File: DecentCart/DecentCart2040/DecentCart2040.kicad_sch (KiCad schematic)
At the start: 74 parts, among them J1 Micro_SD_Card, J2 Conn_02x15_Row_Letter_First, J3 SM03B-SRSS-TB, J7 Conn_01x04, J8 USB_B_Micro, J9 SM03B-SRSS-TB, Q2 TP0610L, SW2 SW_TACTILE, SW3 SW_TACTILE, U1 SN74LVC8T245, U2 SN74LVC8T245, U3 ATtiny1616-M, U4 NCP1117-3.3, U5 SN74LVC8T245, U6 SN74AVC4T245PW, U7 RP2040, U9 W25Q128JVS, X1 12MHz

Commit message: DecentCart 2040 rev. 1.1 fixes
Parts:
- added D3: MBR120VLSFT1G, Diode_SMD:Nexperia_CFP3_SOD-123W, symbol Device:D_Schottky
- Q2: value TP0610L -> DMG2305UX; JLCPCB Part # C10487 -> C150470
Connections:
- net +3V3: now also C14.1
- net +5V HOST: now also C18.2, C19.2, C2.2, C3.2, C30.2, C31.2, C39.2, C40.2, U1.23 (V_{CCB}), U1.24 (V_{CCB}), U2.23 (V_{CCB}), U2.24 (V_{CCB}), U5.23 (V_{CCB}), U5.24 (V_{CCB}), U6.16 (VCCB)
- net GND: now also C14.2
- net GPIO28: now also J7.4 (Pin_4), U3.13 (PB1); no longer J7.3 (Pin_3), U3.14 (PB0)
- net GPIO29: now also J7.3 (Pin_3), U3.14 (PB0); no longer J7.4 (Pin_4), U3.13 (PB1)
- net VBUS: now also D3.2 (A); no longer C26.1, U4.3 (VI)
- removed net +5V: C18.2, C19.2, C2.2, C3.2, C30.2, C31.2, C39.2, C40.2, Q2.1 (S), U1.23 (V_{CCB}), U1.24 (V_{CCB}), U2.23 (V_{CCB}), U2.24 (V_{CCB}), U5.23 (V_{CCB}), U5.24 (V_{CCB}), U6.16 (VCCB)
- new net VSYS: C26.1, D3.1 (K), Q2.1 (S), U4.3 (VI)
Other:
- note removed: "Only use to flash firmware"
- moved on the sheet: C14, Q2

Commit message: DecentCart2040 rev. 1.1
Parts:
- removed U6: SN74AVC4T245PW, Package_SO:TSSOP-16_4.4x5mm_P0.65mm, symbol Logic_LevelTranslator:SN74AVC4T245PW
- added C15, C20: 100nF, Capacitor_SMD:C_0402_1005Metric, symbol Device:C_Small
- added C21: 1uF, Capacitor_SMD:C_0402_1005Metric, symbol Device:C_Small
- added J4: Conn_01x08_Pin, Connector_PinHeader_1.27mm:PinHeader_2x04_P1.27mm_Vertical, symbol Connector:Conn_01x08_Pin
- added U6, U8: SN74LVC2T45DCUR, Package_SO:VSSOP-8_2.3x2mm_P0.5mm, symbol Logic_LevelTranslator:SN74LVC2T45DCUR
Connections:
- net +3V3: now also J3.2 (Pin_2), C15.2, U6.1 (VCCA), U8.1 (VCCA); no longer J3.1 (Pin_1)
- net +5V HOST: now also C20.2, C21.2, U6.8 (VCCB), U8.8 (VCCB)
- net /S4: now also U6.7 (B1)
- net /S5: now also U6.6 (B2)
- net GND: now also J3.3 (Pin_3), C15.1, C20.1, C21.1, U6.4 (GND), U8.4 (GND); no longer J3.2 (Pin_2)
- net GPIO23: now also R1.1
- net GPIO24: now also U6.2 (A1)
- net GPIO25: now also U6.3 (A2)
- net GPIO26: now also U8.2 (A1)
- net GPIO27: now also U8.3 (A2)
- net LVL_EN: now also J4.8 (Pin_8)
- net R/W: no longer R1.1
- net RD4: now also U8.7 (B1)
- net RD5: now also U8.6 (B2)
- net at U3.10 (PB4): now also J4.7 (Pin_7)
- net at U3.11 (PB3): now also J4.6 (Pin_6); no longer D2.1 (K)
- net at U3.12 (PB2): now also J4.5 (Pin_5); no longer R10.1
- net at U3.15 (PC0): now also J4.1 (Pin_1)
- net at U3.16 (PC1): now also J4.2 (Pin_2)
- net at U3.17 (PC2): now also J4.3 (Pin_3)
- net at U3.18 (PC3): now also J4.4 (Pin_4)
- net at U3.19 (~{RESET}/PA0): now also J3.1 (Pin_1); no longer J3.3 (Pin_3)
- net at U3.6 (PA5): now also J1.9 (DET)
- net at U3.7 (PA6): now also R10.1
- net at U3.8 (PA7): now also D1.2 (A), D2.1 (K)
- net at D1.1 (K), D2.2 (A): now also R10.2
- net at R2.2: now also U6.5 (DIR)
- net at R3.2: now also U8.5 (DIR)
- no-connect marks 10 -> 1
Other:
- note added: "Address & Control"
- note added: "Bank Shifting"
- note added: "RP2040"
- note removed: "Address"
- note removed: "I/O"
- moved on the sheet: C1, C10, C11, C12, C13, C14, C16, C17, C18, C19, C2, C23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

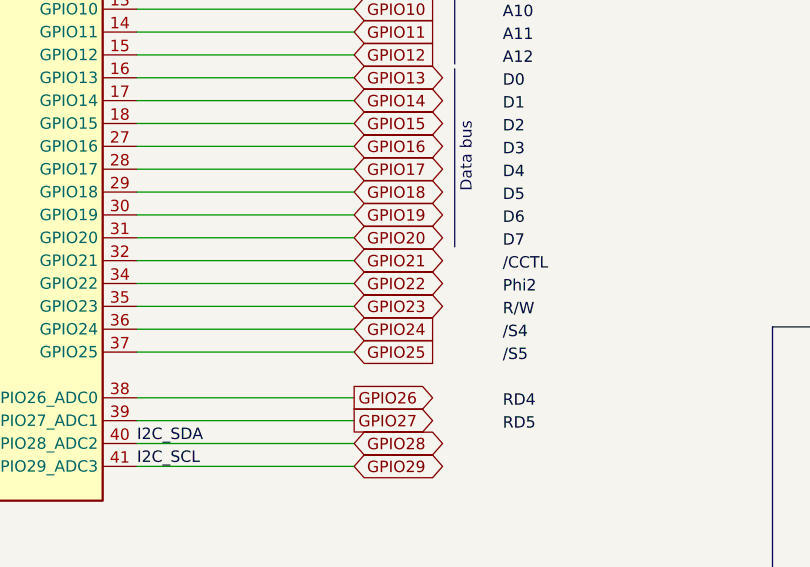
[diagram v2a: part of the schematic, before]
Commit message: DecentCart 2350 component placement
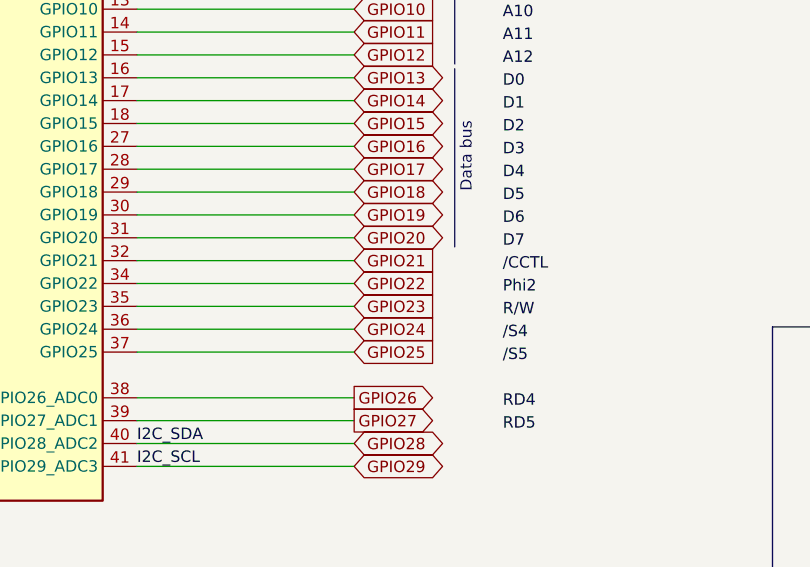
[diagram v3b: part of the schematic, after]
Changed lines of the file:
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@@
 	)
 	(global_label "GPIO22"
-		(shape bidirectional)
+		(shape input)
 		(at 228.6 142.24 0)
 		(fields_autoplaced yes)
@@
 	)
 	(global_label "GPIO21"
-		(shape bidirectional)
+		(shape input)
 		(at 228.6 139.7 0)
 		(fields_autoplaced yes)
@@
 	)
 	(global_label "GPIO23"
-		(shape bidirectional)
+		(shape input)
 		(at 228.6 144.78 0)
 		(fields_autoplaced yes)
